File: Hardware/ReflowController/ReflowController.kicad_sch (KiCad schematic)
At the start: 15 parts, among them J10 2060-1452, J11 2060-1452, J12 RJ45_Display, J13 RJ45_Keypad, J14 Conn_01x03_Socket, J3 2060-1452, J4 2060-1452, J5 2060-1452, J6 2060-1452, J7 2060-1452, J8 2060-1452, J9 2060-1452, Q1 BT136-500, U7 MOC3021M

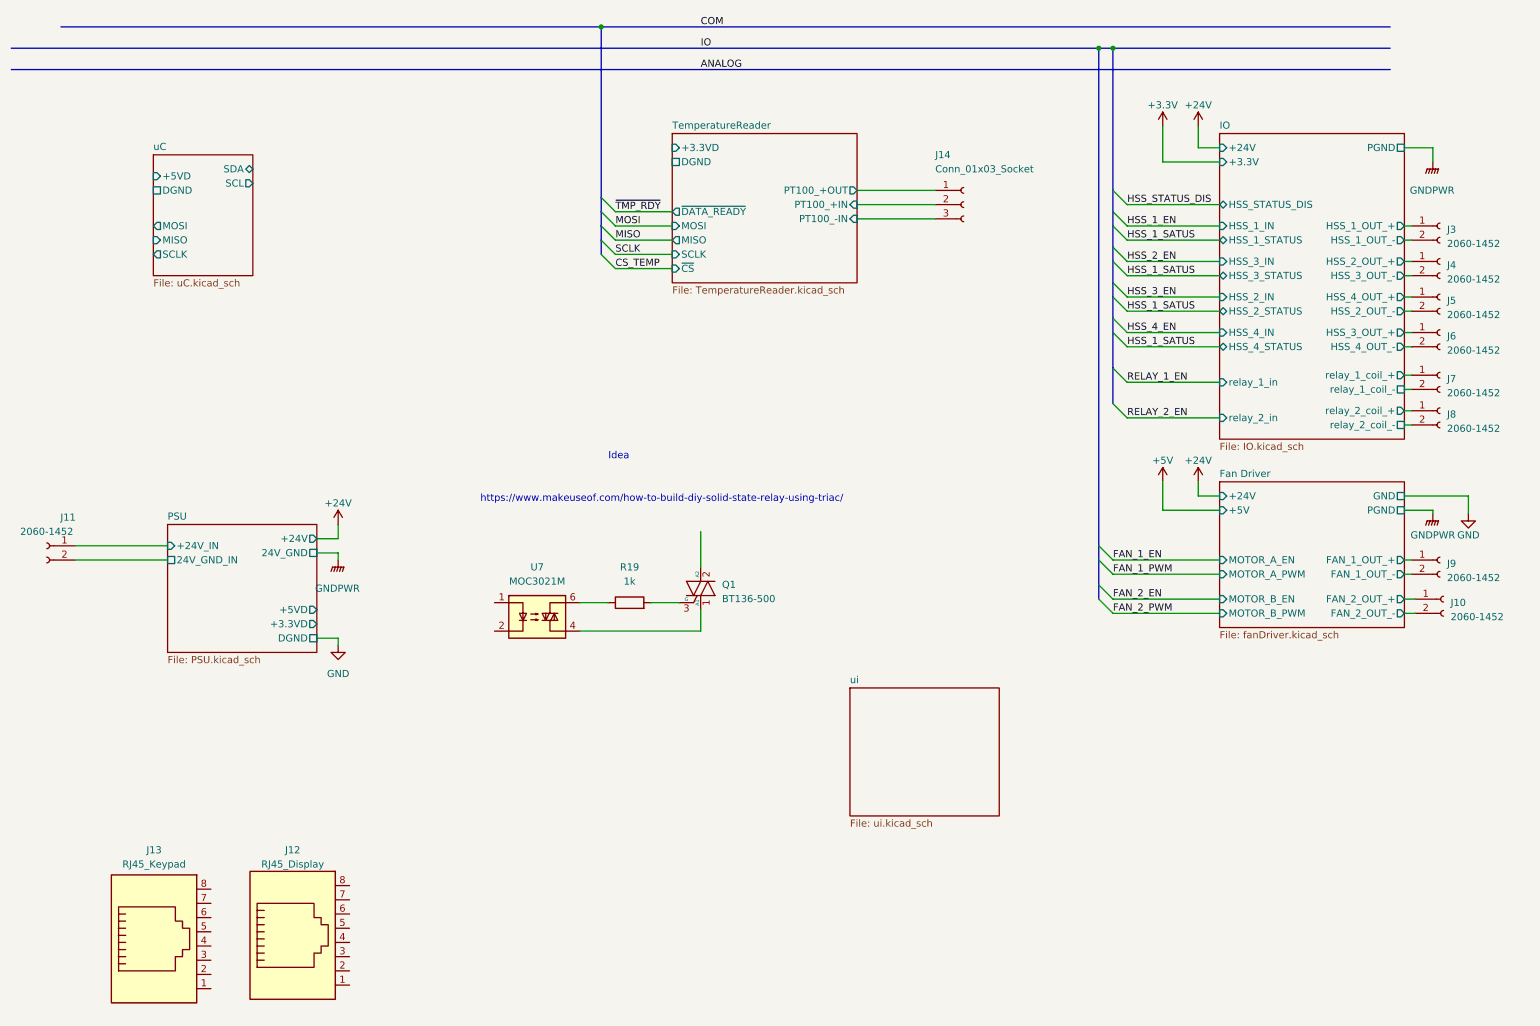
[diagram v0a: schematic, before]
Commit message: finished the io control for the pcb, need to define what is the best way for a remote keypad
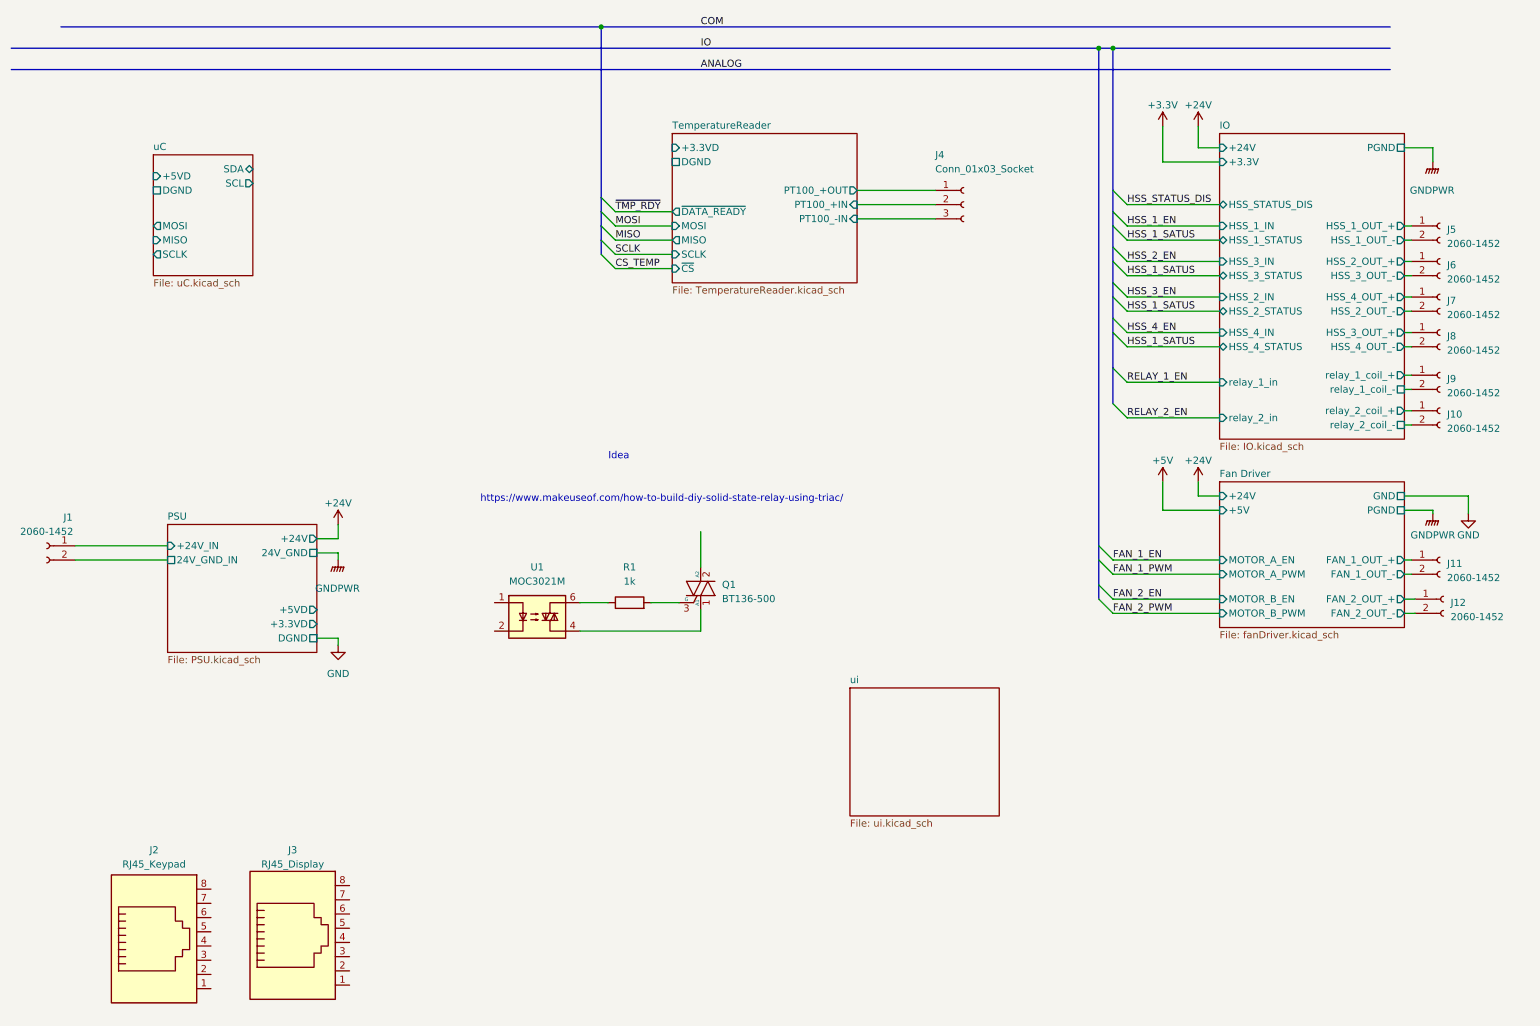
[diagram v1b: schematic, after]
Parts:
- renumbered J11 to J1, J8 to J10, J9 to J11, J10 to J12, J13 to J2, J12 to J3, J14 to J4, J3 to J5, J4 to J6, J5 to J7, J6 to J8, J7 to J9, R19 to R1, U7 to U1
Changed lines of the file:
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@@
   (symbol (lib_id "Connector:Conn_01x02_Socket") (at 267.97 113.03 0) (unit 1)
     (in_bom yes) (on_board yes) (dnp no) (fields_autoplaced)
-    (property "Reference" "J9" (at 269.24 113.665 0)
+    (property "Reference" "J11" (at 269.24 113.665 0)
       (effects (font (size 1.27 1.27)) (justify left))
     )
@@
       (project "ReflowController"
         (path "/2394cc2a-b9b0-4c0b-be11-1fc6085b0d5c"
-          (reference "J9") (unit 1)
+          (reference "J11") (unit 1)
         )
       )
@@
   (symbol (lib_id "Connector:RJ45") (at 62.992 181.356 0) (unit 1)
     (in_bom yes) (on_board yes) (dnp no) (fields_autoplaced)
-    (property "Reference" "J12" (at 62.992 164.846 0)
+    (property "Reference" "J3" (at 62.992 164.846 0)
       (effects (font (size 1.27 1.27)))
     )
@@
       (project "ReflowController"
         (path "/2394cc2a-b9b0-4c0b-be11-1fc6085b0d5c"
-          (reference "J12") (unit 1)
+          (reference "J3") (unit 1)
         )
       )
@@
   (symbol (lib_id "power:GNDPWR") (at 266.7 41.91 0) (unit 1)
     (in_bom yes) (on_board yes) (dnp no) (fields_autoplaced)
-    (property "Reference" "#PWR09" (at 266.7 46.99 0)
+    (property "Reference" "#PWR08" (at 266.7 46.99 0)
       (effects (font (size 1.27 1.27)) hide)
     )
@@
       (project "ReflowController"
         (path "/2394cc2a-b9b0-4c0b-be11-1fc6085b0d5c"
-          (reference "#PWR09") (unit 1)
+          (reference "#PWR08") (unit 1)
         )
       )
@@
   (symbol (lib_id "Device:R") (at 123.19 120.65 90) (unit 1)
     (in_bom yes) (on_board yes) (dnp no) (fields_autoplaced)
-    (property "Reference" "R19" (at 123.19 114.3 90)
+    (property "Reference" "R1" (at 123.19 114.3 90)
       (effects (font (size 1.27 1.27)))
     )
@@
       (project "ReflowController"
         (path "/2394cc2a-b9b0-4c0b-be11-1fc6085b0d5c"
-          (reference "R19") (unit 1)
+          (reference "R1") (unit 1)
         )
       )
@@
   (symbol (lib_id "power:+24V") (at 224.79 99.06 0) (unit 1)
     (in_bom yes) (on_board yes) (dnp no) (fields_autoplaced)
-    (property "Reference" "#PWR06" (at 224.79 102.87 0)
+    (property "Reference" "#PWR07" (at 224.79 102.87 0)
       (effects (font (size 1.27 1.27)) hide)
     )
@@
       (project "ReflowController"
         (path "/2394cc2a-b9b0-4c0b-be11-1fc6085b0d5c"
-          (reference "#PWR06") (unit 1)
+          (reference "#PWR07") (unit 1)
         )
       )
@@
   (symbol (lib_id "power:GND") (at 71.12 128.27 0) (unit 1)
     (in_bom yes) (on_board yes) (dnp no) (fields_autoplaced)
-    (property "Reference" "#PWR02" (at 71.12 134.62 0)
+    (property "Reference" "#PWR03" (at 71.12 134.62 0)
       (effects (font (size 1.27 1.27)) hide)
     )
@@
       (project "ReflowController"
         (path "/2394cc2a-b9b0-4c0b-be11-1fc6085b0d5c"
-          (reference "#PWR02") (unit 1)
+          (reference "#PWR03") (unit 1)
         )
       )
@@
   (symbol (lib_id "Connector:Conn_01x02_Socket") (at 267.97 80.01 0) (unit 1)
     (in_bom yes) (on_board yes) (dnp no) (fields_autoplaced)
-    (property "Reference" "J7" (at 269.24 80.645 0)
+    (property "Reference" "J9" (at 269.24 80.645 0)
       (effects (font (size 1.27 1.27)) (justify left))
     )
@@
       (project "ReflowController"
         (path "/2394cc2a-b9b0-4c0b-be11-1fc6085b0d5c"
-          (reference "J7") (unit 1)
+          (reference "J9") (unit 1)
         )
       )
@@
   (symbol (lib_id "Connector:Conn_01x02_Socket") (at 19.05 110.49 0) (mirror y) (unit 1)
     (in_bom yes) (on_board yes) (dnp no)
-    (property "Reference" "J11" (at 22.86 105.41 0)
+    (property "Reference" "J1" (at 22.86 105.41 0)
       (effects (font (size 1.27 1.27)))
     )
@@
       (project "ReflowController"
         (path "/2394cc2a-b9b0-4c0b-be11-1fc6085b0d5c"
-          (reference "J11") (unit 1)
+          (reference "J1") (unit 1)
         )
       )
@@
   (symbol (lib_id "Relay_SolidState:MOC3021M") (at 106.68 123.19 0) (unit 1)
     (in_bom yes) (on_board yes) (dnp no) (fields_autoplaced)
-    (property "Reference" "U7" (at 106.68 114.3 0)
+    (property "Reference" "U1" (at 106.68 114.3 0)
       (effects (font (size 1.27 1.27)))
     )
@@
       (project "ReflowController"
         (path "/2394cc2a-b9b0-4c0b-be11-1fc6085b0d5c"
-          (reference "U7") (unit 1)
+          (reference "U1") (unit 1)
         )
       )
@@
   (symbol (lib_id "Connector:Conn_01x02_Socket") (at 268.605 120.015 0) (unit 1)
     (in_bom yes) (on_board yes) (dnp no) (fields_autoplaced)
-    (property "Reference" "J10" (at 269.875 120.65 0)
+    (property "Reference" "J12" (at 269.875 120.65 0)
       (effects (font (size 1.27 1.27)) (justify left))
     )
@@
       (project "ReflowController"
         (path "/2394cc2a-b9b0-4c0b-be11-1fc6085b0d5c"
-          (reference "J10") (unit 1)
+          (reference "J12") (unit 1)
         )
       )
@@
   (symbol (lib_id "Connector:Conn_01x02_Socket") (at 267.97 53.34 0) (unit 1)
     (in_bom yes) (on_board yes) (dnp no) (fields_autoplaced)
-    (property "Reference" "J3" (at 269.24 53.975 0)
+    (property "Reference" "J5" (at 269.24 53.975 0)
       (effects (font (size 1.27 1.27)) (justify left))
     )
@@
       (project "ReflowController"
         (path "/2394cc2a-b9b0-4c0b-be11-1fc6085b0d5c"
-          (reference "J3") (unit 1)
+          (reference "J5") (unit 1)
         )
       )
@@
   (symbol (lib_id "power:+24V") (at 224.79 35.56 0) (unit 1)
     (in_bom yes) (on_board yes) (dnp no) (fields_autoplaced)
-    (property "Reference" "#PWR03" (at 224.79 39.37 0)
+    (property "Reference" "#PWR06" (at 224.79 39.37 0)
       (effects (font (size 1.27 1.27)) hide)
     )
@@
       (project "ReflowController"
         (path "/2394cc2a-b9b0-4c0b-be11-1fc6085b0d5c"
-          (reference "#PWR03") (unit 1)
+          (reference "#PWR06") (unit 1)
         )
       )
@@
   (symbol (lib_id "power:GNDPWR") (at 71.12 113.03 0) (unit 1)
     (in_bom yes) (on_board yes) (dnp no) (fields_autoplaced)
-    (property "Reference" "#PWR08" (at 71.12 118.11 0)
+    (property "Reference" "#PWR02" (at 71.12 118.11 0)
       (effects (font (size 1.27 1.27)) hide)
     )
@@
       (project "ReflowController"
         (path "/2394cc2a-b9b0-4c0b-be11-1fc6085b0d5c"
-          (reference "#PWR08") (unit 1)
+          (reference "#PWR02") (unit 1)
         )
       )
@@
   (symbol (lib_id "Connector:RJ45") (at 38.227 181.991 0) (unit 1)
     (in_bom yes) (on_board yes) (dnp no) (fields_autoplaced)
-    (property "Reference" "J13" (at 38.227 164.846 0)
+    (property "Reference" "J2" (at 38.227 164.846 0)
       (effects (font (size 1.27 1.27)))
     )
@@
       (project "ReflowController"
         (path "/2394cc2a-b9b0-4c0b-be11-1fc6085b0d5c"
-          (reference "J13") (unit 1)
+          (reference "J2") (unit 1)
         )
       )
@@
   (symbol (lib_id "Connector:Conn_01x02_Socket") (at 267.97 66.04 0) (unit 1)
     (in_bom yes) (on_board yes) (dnp no) (fields_autoplaced)
-    (property "Reference" "J5" (at 269.24 66.675 0)
+    (property "Reference" "J7" (at 269.24 66.675 0)
       (effects (font (size 1.27 1.27)) (justify left))
     )
@@
       (project "ReflowController"
         (path "/2394cc2a-b9b0-4c0b-be11-1fc6085b0d5c"
-          (reference "J5") (unit 1)
+          (reference "J7") (unit 1)
         )
       )
@@
   (symbol (lib_id "power:GNDPWR") (at 266.7 104.775 0) (unit 1)
     (in_bom yes) (on_board yes) (dnp no)
-    (property "Reference" "#PWR07" (at 266.7 109.855 0)
+    (property "Reference" "#PWR09" (at 266.7 109.855 0)
       (effects (font (size 1.27 1.27)) hide)
     )
@@
       (project "ReflowController"
         (path "/2394cc2a-b9b0-4c0b-be11-1fc6085b0d5c"
-          (reference "#PWR07") (unit 1)
+          (reference "#PWR09") (unit 1)
         )
       )
@@
   (symbol (lib_id "Connector:Conn_01x02_Socket") (at 267.97 72.39 0) (unit 1)
     (in_bom yes) (on_board yes) (dnp no) (fields_autoplaced)
-    (property "Reference" "J6" (at 269.24 73.025 0)
+    (property "Reference" "J8" (at 269.24 73.025 0)
       (effects (font (size 1.27 1.27)) (justify left))
     )
@@
       (project "ReflowController"
         (path "/2394cc2a-b9b0-4c0b-be11-1fc6085b0d5c"
-          (reference "J6") (unit 1)
+          (reference "J8") (unit 1)
         )
       )
@@
   (symbol (lib_id "Connector:Conn_01x02_Socket") (at 267.97 59.69 0) (unit 1)
     (in_bom yes) (on_board yes) (dnp no) (fields_autoplaced)
-    (property "Reference" "J4" (at 269.24 60.325 0)
+    (property "Reference" "J6" (at 269.24 60.325 0)
       (effects (font (size 1.27 1.27)) (justify left))
     )
@@
       (project "ReflowController"
         (path "/2394cc2a-b9b0-4c0b-be11-1fc6085b0d5c"
-          (reference "J4") (unit 1)
+          (reference "J6") (unit 1)
         )
       )
@@
   (symbol (lib_id "Connector:Conn_01x02_Socket") (at 267.97 86.36 0) (unit 1)
     (in_bom yes) (on_board yes) (dnp no) (fields_autoplaced)
-    (property "Reference" "J8" (at 269.24 86.995 0)
+    (property "Reference" "J10" (at 269.24 86.995 0)
       (effects (font (size 1.27 1.27)) (justify left))
     )
@@
       (project "ReflowController"
         (path "/2394cc2a-b9b0-4c0b-be11-1fc6085b0d5c"
-          (reference "J8") (unit 1)
+          (reference "J10") (unit 1)
         )
       )
@@
   (symbol (lib_id "Connector:Conn_01x03_Socket") (at 182.88 49.53 0) (unit 1)
     (in_bom yes) (on_board yes) (dnp no)
-    (property "Reference" "J14" (at 177.8 40.64 0)
+    (property "Reference" "J4" (at 177.8 40.64 0)
       (effects (font (size 1.27 1.27)) (justify left))
     )
@@
       (project "ReflowController"
         (path "/2394cc2a-b9b0-4c0b-be11-1fc6085b0d5c"
-          (reference "J14") (unit 1)
-        )
-      )
+          (reference "J4") (unit 1)
+        )
+      )

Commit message: Wrking with edwin on the hwole schematic
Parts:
- removed J2: RJ45_Keypad, Connector_RJ:RJ45_Amphenol_54602-x08_Horizontal, symbol Connector:RJ45
- removed J3: RJ45_Display, Connector_RJ:RJ45_Amphenol_54602-x08_Horizontal, symbol Connector:RJ45
- removed Q1: BT136-500, Package_TO_SOT_THT:TO-220-3_Vertical, symbol Triac_Thyristor:BT136-500
- removed R1: 1k, Resistor_SMD:R_1206_3216Metric, symbol Device:R
- removed U1: MOC3021M, symbol Relay_SolidState:MOC3021M
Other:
- note removed: "Idea"
- note removed: "https://www.makeuseof.com/how-to-build-diy-solid-state-relay-using-triac/"
